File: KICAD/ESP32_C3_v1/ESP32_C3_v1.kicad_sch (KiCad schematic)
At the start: 32 parts, among them J1 USB Serial/JTAG, J10 Peer_UART, J2 Port_Header, J3 Grove I2C, J4 ADC_Header, J5 Screw_Terminal_01x03, J6 Screw_Terminal_01x03, J7 J_AUTO (Reset Automation), J8 External 5V Power, J9 SPI (Optional Module Flash), U1 ESP32-C3-DevKitC-02, U2 MCP23008-xP, U3 MCP3008

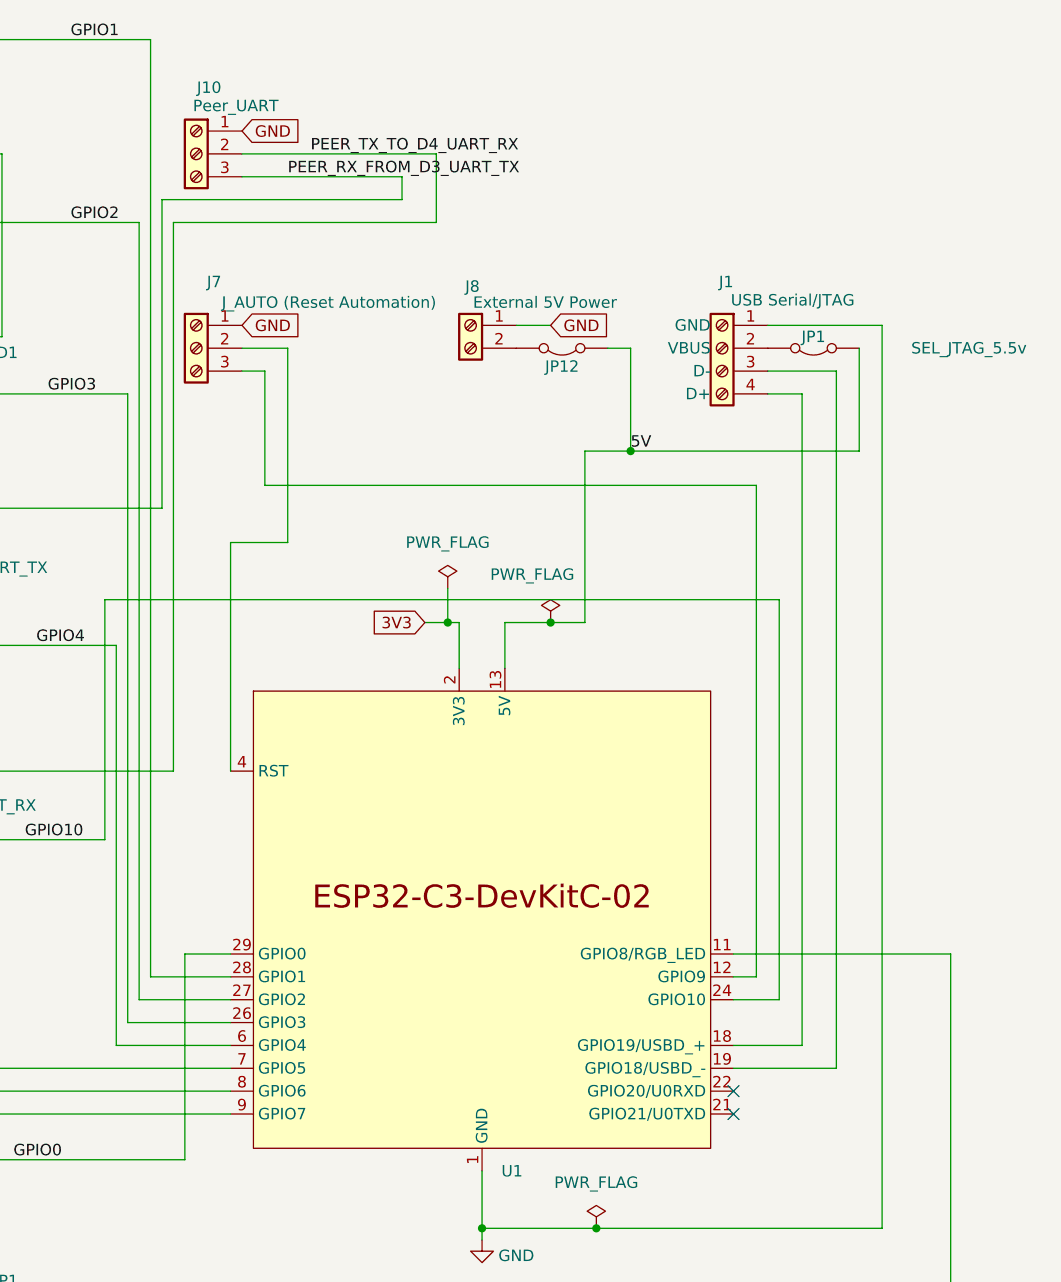
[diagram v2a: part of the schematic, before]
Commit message: Add ESP32-C3 schematic v1.1 UART crosslink
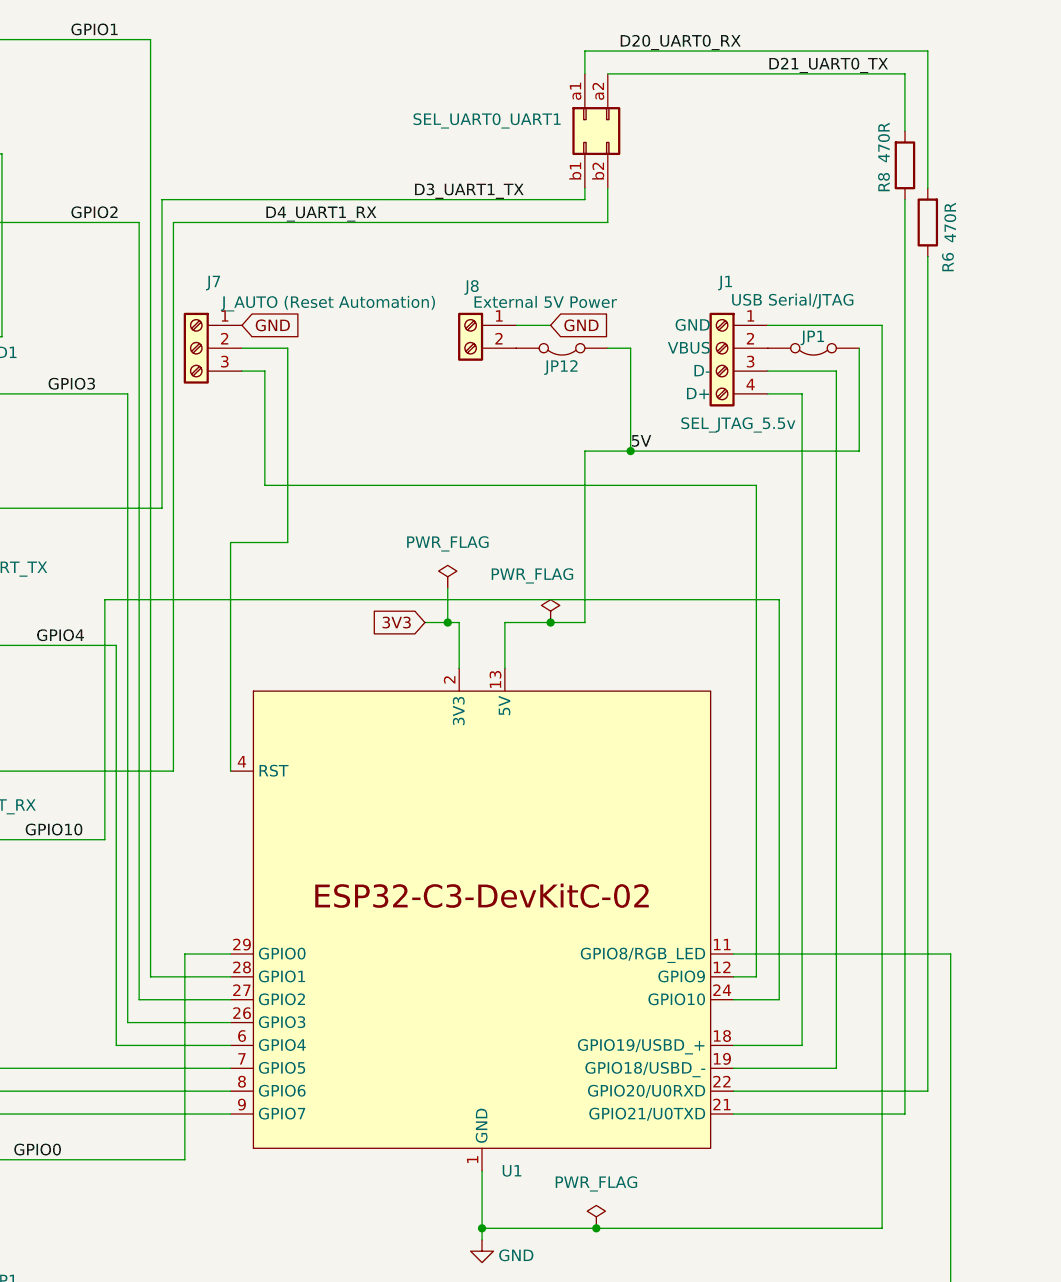
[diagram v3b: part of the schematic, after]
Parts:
- removed J10: Peer_UART, ESP32_C3_Harness:TerminalBlock_Phoenix_MPT-0,5-3-2.54_1x03_P2.54mm_Horizontal, symbol ESP32_C3_Harness:Screw_Terminal_01x03
- added R6, R8: 470R, ESP32_C3_Harness:R_Axial_DIN0411_L9.9mm_D3.6mm_P5.08mm_Vertical, symbol ESP32_C3_Harness:Resistor
- added SEL_UART0_UART1: D3TX-D20RX | D21TX-D4RX, ESP32_C3_Harness:PinHeader_2x02_RowLetter_P2.54mm_Vertical, symbol ESP32_C3_Harness:Conn_02x02_Row_Letter_First
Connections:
- net at U1.21 (GPIO21/U0TXD): now also R8.1
- net at U1.22 (GPIO20/U0RXD): now also R6.1
- net PEER_RX_FROM_D3_UART_TX renamed D3_UART1_TX
- net D3_UART1_TX: now also SEL_UART0_UART1.b1 (Pin_b1)
- net PEER_TX_TO_D4_UART_RX renamed D4_UART1_RX
- net D4_UART1_RX: now also SEL_UART0_UART1.b2 (Pin_b2)
- new net D20_UART0_RX: R6.2, SEL_UART0_UART1.a1 (Pin_a1)
- new net D21_UART0_TX: R8.2, SEL_UART0_UART1.a2 (Pin_a2)
- no-connect marks 2 -> 0

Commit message: Refine ESP32-C3 v1.1 J10 UART schematic and PCB
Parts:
- removed SEL_UART0_UART1: D3TX-D20RX | D21TX-D4RX, ESP32_C3_Harness:PinHeader_2x02_RowLetter_P2.54mm_Vertical, symbol ESP32_C3_Harness:Conn_02x02_Row_Letter_First
- added J10: SEL_UART0_UART1, ESP32_C3_Harness:PinHeader_2x03_RowLetter_P2.54mm_Vertical, symbol ESP32_C3_Harness:Conn_02x03_Row_Letter_First
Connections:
- net D20_UART0_RX: now also J10.a1 (Pin_a1)
- net D21_UART0_TX: now also J10.a2 (Pin_a2)
- net D3_UART1_TX: now also J10.b1 (Pin_b1)
- net D4_UART1_RX: now also J10.b2 (Pin_b2)
- net GND: now also J10.a3 (Pin_a3), J10.b3 (Pin_b3)
- net GPIO09: now reaches J7.3 (Pin_3), U1.12 (GPIO9)
- net Reset: now reaches J7.2 (Pin_2), U1.4 (RST)
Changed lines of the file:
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@@
 	)
 	(junction
+		(at 252.73 16.51)
+		(diameter 0)
+		(color 0 0 0 0)
+	)
+	(junction
 		(at 101.6 130.81)
 		(diameter 0)
@@
 	)
 	(junction
+		(at 245.11 24.13)
+		(diameter 0)
+		(color 0 0 0 0)
+	)
+	(junction
 		(at 220.98 146.05)
 		(diameter 0)
@@
 	(wire
 		(pts
+			(xy 234.95 17.78) (xy 234.95 16.51)
+		)
+		(stroke
+			(width 0)
+			(type default)
+		)
+	)
+	(wire
+		(pts
 			(xy 149.86 26.67) (xy 151.13 26.67)
 		)
@@
 	(wire
 		(pts
+			(xy 234.95 16.51) (xy 252.73 16.51)
+		)
+		(stroke
+			(width 0)
+			(type default)
+		)
+	)
+	(wire
+		(pts
 			(xy 254 120.65) (xy 254 76.2)
 		)
@@
 	(wire
 		(pts
+			(xy 252.73 16.51) (xy 267.97 16.51)
+		)
+		(stroke
+			(width 0)
+			(type default)
+		)
+	)
+	(wire
+		(pts
 			(xy 40.64 134.62) (xy 49.53 134.62)
 		)
@@
 	(wire
 		(pts
-			(xy 267.97 17.78) (xy 267.97 24.13)
+			(xy 267.97 16.51) (xy 267.97 24.13)
 		)
 		(stroke
@@
 	(wire
 		(pts
-			(xy 234.95 17.78) (xy 267.97 17.78)
-		)
-		(stroke
-			(width 0)
-			(type default)
-		)
-	)
-	(wire
-		(pts
 			(xy 187.96 115.57) (xy 193.04 115.57)
 		)
@@
 	(wire
 		(pts
+			(xy 245.11 24.13) (xy 245.11 30.48)
+		)
+		(stroke
+			(width 0)
+			(type default)
+		)
+	)
+	(wire
+		(pts
 			(xy 96.52 67.31) (xy 96.52 109.22)
 		)
@@
 	(wire
 		(pts
+			(xy 245.11 30.48) (xy 237.49 30.48)
+		)
+		(stroke
+			(width 0)
+			(type default)
+		)
+	)
+	(wire
+		(pts
 			(xy 232.41 31.75) (xy 232.41 30.48)
 		)
@@
 	(wire
 		(pts
+			(xy 245.11 24.13) (xy 247.65 24.13)
+		)
+		(stroke
+			(width 0)
+			(type default)
+		)
+	)
+	(wire
+		(pts
+			(xy 237.49 17.78) (xy 245.11 17.78)
+		)
+		(stroke
+			(width 0)
+			(type default)
+		)
+	)
+	(wire
+		(pts
 			(xy 102.87 80.01) (xy 80.01 80.01)
 		)
@@
 	(wire
 		(pts
+			(xy 245.11 17.78) (xy 245.11 24.13)
+		)
+		(stroke
+			(width 0)
+			(type default)
+		)
+	)
+	(wire
+		(pts
 			(xy 62.23 124.46) (xy 62.23 128.27)
 		)
@@
 	(wire
 		(pts
+			(xy 252.73 19.05) (xy 252.73 16.51)
+		)
+		(stroke
+			(width 0)
+			(type default)
+		)
+	)
+	(wire
+		(pts
 			(xy 72.39 83.82) (xy 74.93 83.82)
 		)
@@
 		)
 	)
+	(label "Reset"
+		(at 199.39 57.15 0)
+		(effects
+			(font
+				(size 1.27 1.27)
+			)
+			(justify left bottom)
+		)
+	)
 	(label "I2C_A_SDA"
 		(at 129.54 26.67 0)
@@
 		)
 	)
+	(label "GPIO09"
+		(at 208.28 63.5 0)
+		(effects
+			(font
+				(size 1.27 1.27)
+			)
+			(justify left bottom)
+		)
+	)
 	(label "ONEWIRE_DQ"
 		(at 125.73 151.13 0)
@@
 	)
 	(label "D21_UART0_TX"
-		(at 252.73 17.78 0)
+		(at 252.73 19.05 0)
 		(effects
 			(font
@@
 	(global_label "GND"
 		(shape input)
+		(at 247.65 24.13 0)
+		(fields_autoplaced yes)
+		(effects
+			(font
+				(size 1.27 1.27)
+			)
+			(justify left)
+		)
+		(property "Intersheetrefs" "${INTERSHEET_REFS}"
+			(at 254.5057 24.13 0)
+			(effects
+				(font
+					(size 1.27 1.27)
+				)
+				(justify left)
+				(hide yes)
+			)
+		)
+	)
+	(global_label "GND"
+		(shape input)
 		(at 228.6 45.72 0)
 		(fields_autoplaced yes)
@@
 	)
 	(symbol
-		(lib_name "Conn_02x02_Row_Letter_First_3")
-		(lib_id "ESP32_C3_Harness:Conn_02x02_Row_Letter_First")
-		(at 232.41 22.86 90)
-		(mirror x)
-		(unit 1)
-		(exclude_from_sim no)
-		(in_bom yes)
-		(on_board yes)
-		(dnp no)
-		(property "Reference" "SEL_UART0_UART1"
-			(at 229.87 22.8599 90)
-			(effects
-				(font
-					(size 1.27 1.27)
-				)
-				(justify left)
-			)
-		)
-		(property "Value" "D3TX-D20RX | D21TX-D4RX"
-			(at 246.634 33.528 90)
-			(effects
-				(font
-					(size 1.27 1.27)
-				)
-				(justify left)
-				(hide yes)
-			)
-		)
-		(property "Footprint" "ESP32_C3_Harness:PinHeader_2x02_RowLetter_P2.54mm_Vertical"
-			(at 232.41 22.86 0)
-			(effects
-				(font
-					(size 1.27 1.27)
-				)
-				(hide yes)
-			)
-		)
-		(property "Datasheet" "~"
-			(at 232.41 22.86 0)
-			(effects
-				(font
-					(size 1.27 1.27)
-				)
-				(hide yes)
-			)
-		)
-		(property "Description" "Generic connector, double row, 02x02, row letter first pin numbering scheme (pin number consists of a letter for the row and a number for the pin index in this row. a1, ..., aN; b1, ..., bN), script generated (kicad-library-utils/schlib/autogen/connector/)"
-			(at 232.41 22.86 0)
-			(effects
-				(font
-					(size 1.27 1.27)
-				)
-				(hide yes)
-			)
-		)
-		(pin "a1"
-		)
-		(pin "b2"
-		)
-		(pin "b1"
-		)
-		(pin "a2"
-		)
-		(instances
-			(project "ESP32_C3_v1"
-				(path "/31f8d3b5-36d0-4e19-8e74-b3daeb7826ed"
-					(reference "SEL_UART0_UART1")
-					(unit 1)
-				)
-			)
-		)
-	)
-	(symbol
 		(lib_name "Conn_02x02_Row_Letter_First_1")
 		(lib_id "ESP32_C3_Harness:Conn_02x02_Row_Letter_First")
@@
 					(unit 1)
 				)
+			)
+		)
+	)
+	(symbol
+		(lib_id "ESP32_C3_Harness:Conn_02x03_Row_Letter_First")
+		(at 234.95 22.86 90)
+		(mirror x)
+		(unit 1)
+		(exclude_from_sim no)
+		(in_bom yes)
+		(on_board yes)
+		(dnp no)
+		(property "Reference" "J10"
+			(at 229.87 22.8599 90)
+			(effects
+				(font
+					(size 1.27 1.27)
+				)
+				(justify left)
+			)
+		)
+		(property "Value" "SEL_UART0_UART1"
+			(at 229.87 25.3999 90)
+			(effects
+				(font
+					(size 1.27 1.27)
+				)
+				(justify left)
+			)
+		)
+		(property "Footprint" "ESP32_C3_Harness:PinHeader_2x03_RowLetter_P2.54mm_Vertical"
+			(at 234.95 22.86 0)
+			(effects
+				(font
+					(size 1.27 1.27)
+				)
+				(hide yes)
+			)
+		)
+		(property "Datasheet" "~"
+			(at 234.95 22.86 0)
+			(effects
+				(font
+					(size 1.27 1.27)
+				)
+				(hide yes)
+			)
+		)
+		(property "Description" "Generic connector, double row, 02x03, row letter first pin numbering scheme (pin number consists of a letter for the row and a number for the pin index in this row. a1, ..., aN; b1, ..., bN), script generated (kicad-library-utils/schlib/autogen/connector/)"
+			(at 234.95 22.86 0)
+			(effects
+				(font
+					(size 1.27 1.27)
+				)
+				(hide yes)
+			)
+		)
+		(pin "a2"
+		)
+		(pin "a3"
+		)
+		(pin "a1"
+		)
+		(pin "b1"
+		)
+		(pin "b3"
+		)
+		(pin "b2"
+		)
+		(instances
+			(project ""
+				(path "/31f8d3b5-36d0-4e19-8e74-b3daeb7826ed"
+					(reference "J10")
+					(unit 1)
+				)
